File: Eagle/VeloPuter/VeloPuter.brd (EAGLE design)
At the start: 99.1 x 61 mm, 39 parts, among them IC1 LM2931T-L

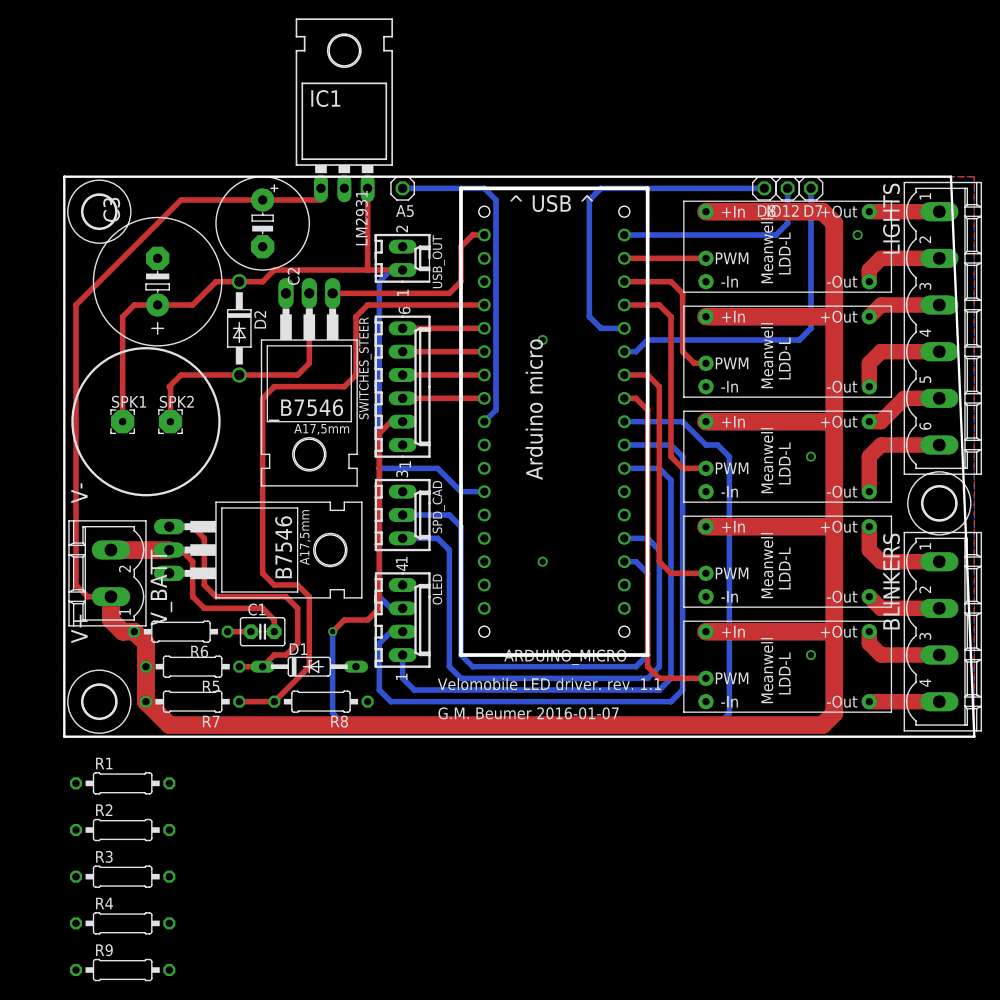
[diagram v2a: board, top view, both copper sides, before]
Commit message: new board layout
has to be checked. Pin changes NOT documented
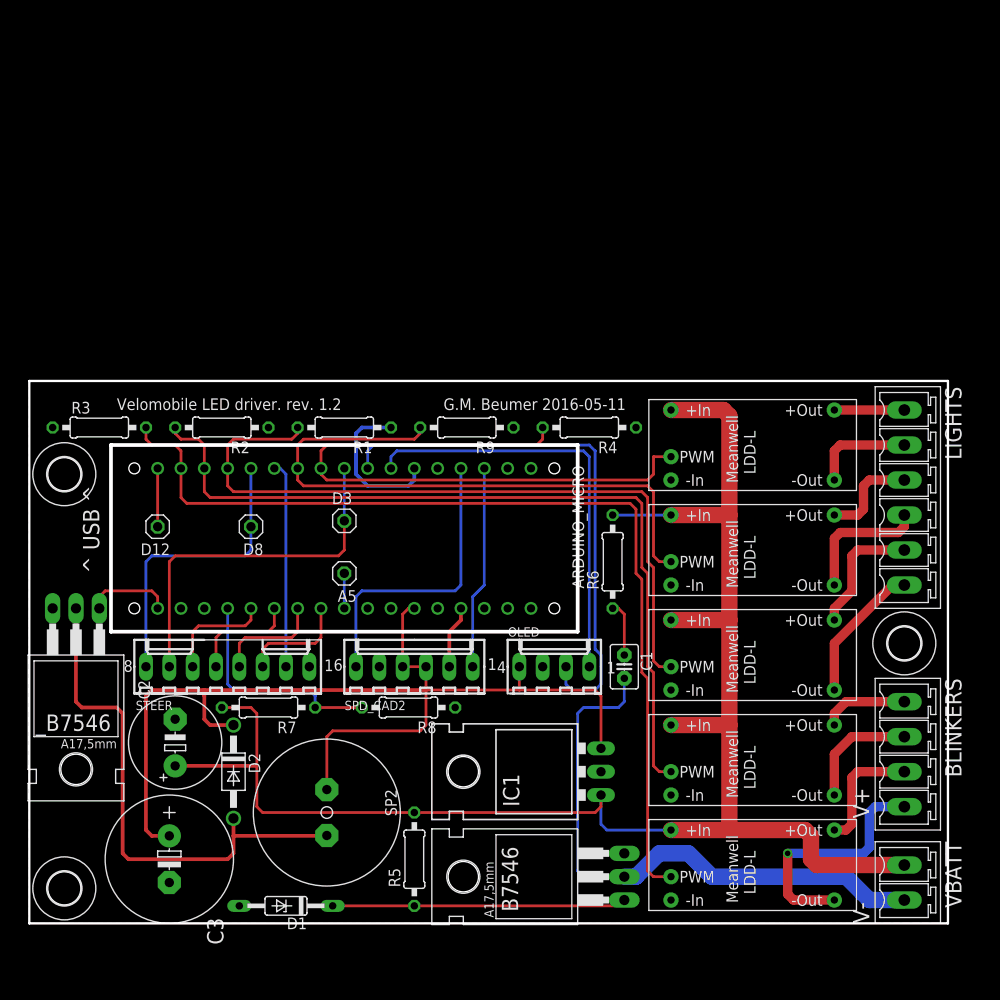
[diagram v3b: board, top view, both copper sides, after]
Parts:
- removed D7, IO12: (no value), pinhead:1X01
- removed SPD_CAD: (no value), con-molex:6410-03
- removed SPK1, SPK2: 0, wirepad:2,54/0,8
- removed SWITCHES_STEER: (no value), con-molex:6410-06
- removed USB_OUT: (no value), con-molex:6410-02
- removed V_BATT: (no value), con-phoenix-508:MSTBV2
- added D12: D12, pinhead:1X01
- added D3: D3, pinhead:1X01
- added SP2: SD1607, TDK_SD1607:AL60P
- added SPD_CAD2: 22-27-2061-06, con-molex:6410-06
- added STEER: 22-27-2081-08, con-molex:6410-08
- added VBATT: MCV2, con-phoenix_3.81_mcv:MCV2
- BLINKERS: value (none) -> 0; device con-phoenix-508:MSTBV4 -> con-phoenix_3.81_mcv:MCV4
- D8: value (none) -> D8
- LIGHTS: value (none) -> 0; device con-phoenix-508:MSTBV6 -> con-phoenix_3.81_mcv:MCV6
- moved R4 74.1 mm to (61.0, 54.0), turned to 180 degrees
- moved IC1 71.5 mm to (58.4, 16.5), turned to 90 degrees
- moved R9 69.9 mm to (47.6, 54.0), turned to 180 degrees
- moved D8 66.9 mm to (24.1, 43.2)
- moved C3 62.9 mm to (15.2, 6.99), turned to 270 degrees
- moved ARDUINO_MICRO 59.1 mm to (12.7, 50.8), turned to 270 degrees
- moved C2 57.3 mm to (15.9, 19.7), turned to 90 degrees
- moved B7546 51.2 mm to (58.4, 5.08), turned to 90 degrees
- moved R3 49.0 mm to (7.62, 54.0)
- moved D2 48.3 mm to (22.2, 16.5)
- moved R6 47.6 mm to (63.5, 39.4), turned to 90 degrees
- moved R1 45.6 mm to (34.3, 54.0), turned to 180 degrees
- moved R2 45.1 mm to (21.0, 54.0), turned to 180 degrees
- moved _B7546 42.7 mm to (5.08, 27.9)
- moved A5 42.4 mm to (34.3, 38.1)
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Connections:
- net A5 renamed FREE_A5
- removed net IO12: ARDUINO_MICRO.D12, IO12.1
- removed net N$16: ARDUINO_MICRO.D7, D7.1
- removed net N$17: ARDUINO_MICRO.D8, D8.1
- new net FREE_D12: ARDUINO_MICRO.D12, D12.1
- new net FREE_D4: ARDUINO_MICRO.D4, D3.1, STEER.7
- new net FREE_D8: ARDUINO_MICRO.D8, D8.1, STEER.8
- net 5V: now also OLED.4, SP2.1, SPD_CAD2.3, SPD_CAD2.4; no longer OLED.3, SPK1.1, USB_OUT.1
- net BRAKE_SWITCH: now also ARDUINO_MICRO.D7, STEER.2; no longer ARDUINO_MICRO.D4, SWITCHES_STEER.2
- net CAD_SWITCH: now also SPD_CAD2.6; no longer SPD_CAD.1
- net DOWN_SWITCH: now also STEER.4; no longer SWITCHES_STEER.4
- net GND: now also OLED.3, SPD_CAD2.2, SPD_CAD2.5, STEER.1; no longer OLED.4, SPD_CAD.3, SWITCHES_STEER.1, USB_OUT.2
- net LEFT_SWITCH: now also STEER.5; no longer SWITCHES_STEER.5
- net N$14: now also SP2.2; no longer SPK2.1
- net N$2: now also VBATT.2; no longer V_BATT.2
- net PWM_FRONT1: now also ARDUINO_MICRO.D5; no longer ARDUINO_MICRO.D11
- net PWM_FRONT2: now also ARDUINO_MICRO.D6; no longer ARDUINO_MICRO.D10
- net PWM_LEFT: now also ARDUINO_MICRO.D10; no longer ARDUINO_MICRO.D6
- net PWM_RIGHT: now also ARDUINO_MICRO.D11; no longer ARDUINO_MICRO.D5
- net RIGHT_SWITCH: now also STEER.6; no longer SWITCHES_STEER.6
- net UP_SWITCH: now also STEER.3; no longer SWITCHES_STEER.3
- net V+: now also VBATT.1; no longer V_BATT.1
- net WHEEL_SWITCH: now also SPD_CAD2.1; no longer SPD_CAD.2
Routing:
- net V+: track 281.5 -> 179.6 mm
- net BRAKE_SWITCH: track 122.3 -> 22.5 mm, vias 1 -> 0
- net PWM_RIGHT: track 37.9 -> 103.4 mm
- net PWM_FRONT1: track 8.89 -> 69.6 mm
- net PWM_LEFT: track 29.0 -> 88.8 mm
- net PWM_BRAKE: track 25.2 -> 79.7 mm
- net PWM_FRONT2: track 16.3 -> 66.7 mm
- net V_0: track 74.1 -> 24.7 mm
- net FREE_D4: track 0.00 -> 39.9 mm
- net N$2: track 24.4 -> 64.3 mm
- net N$16: track 36.6 -> 0.00 mm
- net N$17: track 36.6 -> 0.00 mm
- net FREE_D8: track 0.00 -> 32.3 mm
- net WHEEL_SWITCH: track 54.2 -> 22.1 mm
- net FREE_A5: track 35.3 -> 3.81 mm
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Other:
- board size 99.1 x 61 mm -> 100 x 59 mm
- board text added: "G.M. Beumer 2016-05-11"
- board text added: "Velomobile LED driver. rev. 1.2"
- board text removed: "Arduino micro"
- board text removed: "D4"
- board text removed: "D7"
- board text removed: "G.M. Beumer 2016-01-07"
- board text removed: "IO12"
- board text removed: "IO8"
- board text removed: "LM2931"
- board text removed: "NC7"
- board text removed: "NC8"
- board text removed: "Velomobile LED driver. rev. 1.1"
- board text removed: "led+"
- board text removed: "led-"

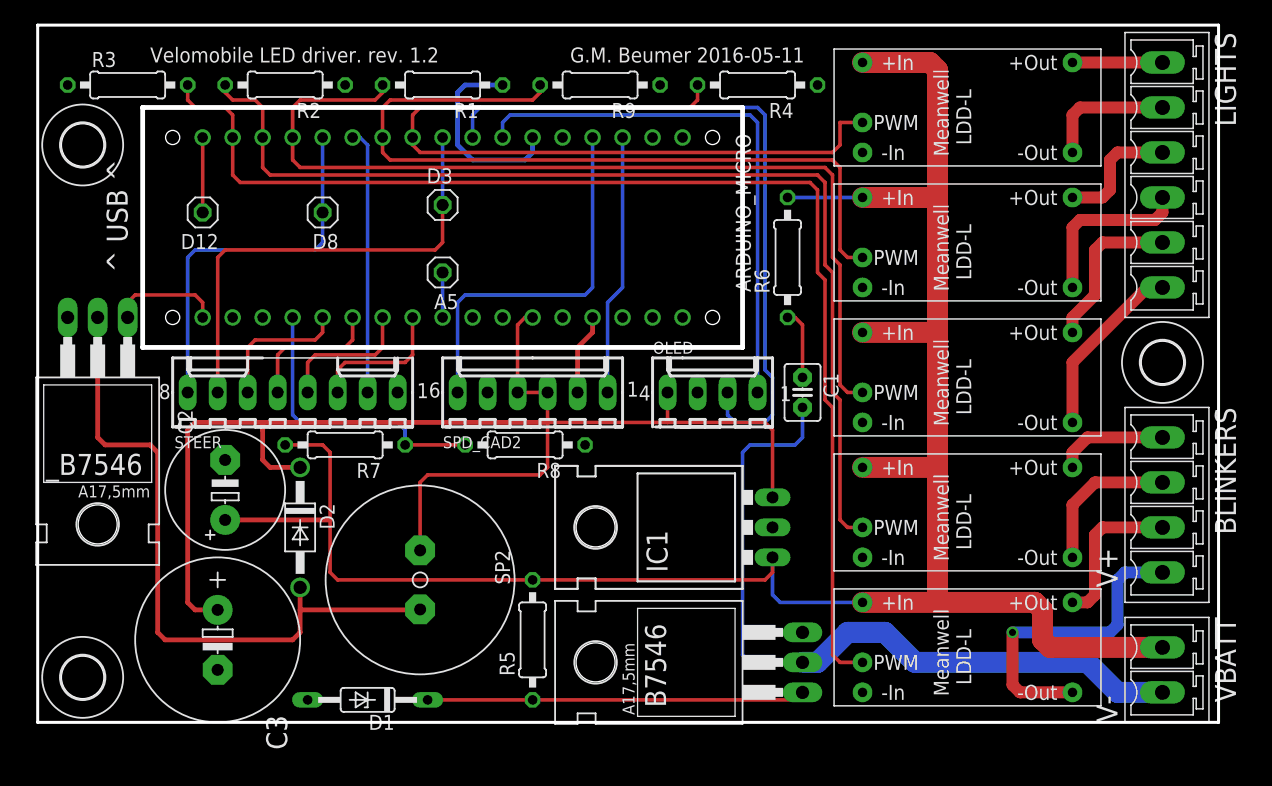
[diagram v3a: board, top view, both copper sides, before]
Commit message: Version of the Veloputer PCB as made as version 1.2 (number of the PCB).
This version is uploaded to seeedstudio.com on 2016-02-21.
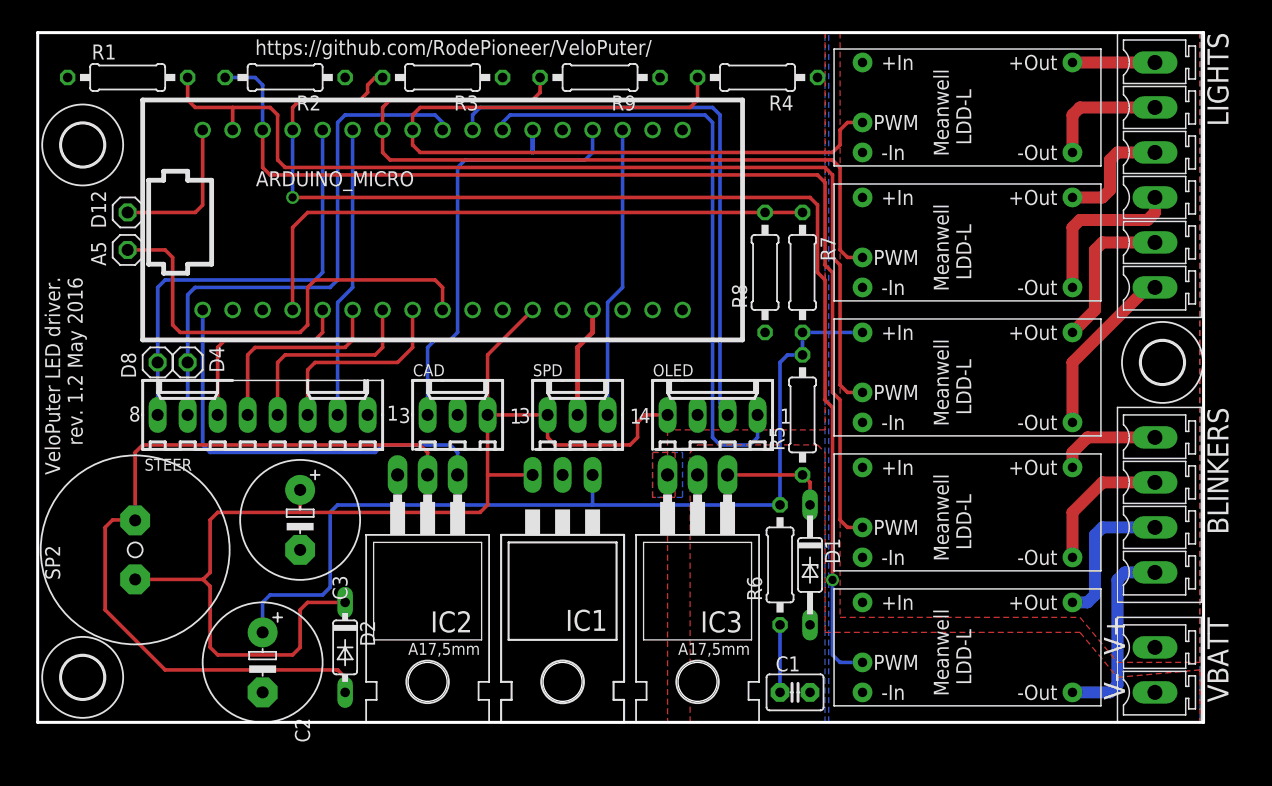
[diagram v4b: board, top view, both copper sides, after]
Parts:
- removed B7546, _B7546: (no value), transistor-power:TO220BH
- removed D3: D3, pinhead:1X01
- removed SPD_CAD2: 22-27-2061-06, con-molex:6410-06
- added CAD, SPD: 22-27-2031-03, con-molex:6410-03
- added D4: (no value), pinhead:1X01
- added IC2, IC3: B7546, transistor-power:TO220BH
- A5: value A5 -> (none)
- ARDUINO_MICRO: value (none) -> ARDUINO_MICROFOOTPRINT; device arduino-micro:ARDUINO-MICRO -> arduino-micro_gbeu:ARDUINO-MICRO
- BLINKERS, LIGHTS: value 0 -> (none)
- C3: device resistor:E5-13 -> resistor:E5-10,5
- D12: value D12 -> (none)
- D2: device diode:DO41-10 -> diode:DO35-7
- D8: value D8 -> (none)
- IC1: value LM2931T-L -> LM2931; device v-reg-3:TO220L1 -> v-reg-3-gbeu:TO220L1
- R9: value 100l -> 100k
- STEER: value 22-27-2081-08 -> (none)
- VBATT: value MCV2 -> (none)
- moved R7 41.4 mm to (64.8, 38.1), turned to 270 degrees
- moved D1 39.2 mm to (65.4, 13.3), turned to 270 degrees
- moved R5 29.8 mm to (64.8, 26.0)
- moved A5 26.7 mm to (7.62, 40.0), turned to 90 degrees
- moved R1 26.7 mm to (7.62, 54.6), turned to 0 degrees
- moved R3 26.7 mm to (34.3, 54.6), turned to 180 degrees
- moved R6 26.0 mm to (62.9, 13.3)
- moved C1 25.4 mm to (64.1, 2.54), turned to 0 degrees
- moved R8 25.0 mm to (61.6, 38.1), turned to 90 degrees
- moved SP2 24.3 mm to (8.26, 14.6), turned to 90 degrees
- moved D8 18.9 mm to (10.2, 30.5), turned to 90 degrees
- moved C2 14.9 mm to (19.1, 5.08), turned to 270 degrees
- moved IC1 14.1 mm to (44.5, 14.6), turned to 180 degrees
- moved C3 12.3 mm to (22.2, 17.1)
- moved D2 10.9 mm to (26.0, 6.35)
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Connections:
- removed net N$2: B7546.D, C1.2, VBATT.2
- new net V-: C1.2, IC3.D, VBATT.2
- net 5V: now also CAD.1, SPD.3; no longer SPD_CAD2.3, SPD_CAD2.4
- net CAD_SWITCH: now also CAD.3; no longer SPD_CAD2.6
- net FREE_D4: now also D4.1; no longer D3.1
- net GND: now also CAD.2, IC2.S, IC3.S, SPD.2; no longer B7546.S, SPD_CAD2.2, SPD_CAD2.5, _B7546.S
- net N$14: now also IC2.D; no longer _B7546.D
- net N$4: now also IC3.G; no longer B7546.G
- net PWM_BRAKE: now also ARDUINO_MICRO.D11; no longer ARDUINO_MICRO.D9
- net PWM_BUZZER: now also IC2.G; no longer _B7546.G
- net PWM_RIGHT: now also ARDUINO_MICRO.D9; no longer ARDUINO_MICRO.D11
- net WHEEL_SWITCH: now also SPD.1; no longer SPD_CAD2.1
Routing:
- net V+: track 179.6 -> 77.3 mm
- net N$2: track 64.3 -> 0.00 mm
- net FREE_A5: track 3.81 -> 38.8 mm
- net PWM_BUZZER: track 9.42 -> 35.7 mm
- net V_0: track 24.7 -> 50.7 mm
- net N$4: track 32.0 -> 9.15 mm
- net 5V: track 115.5 -> 99.5 mm
- net GND: track 23.8 -> 11.3 mm
- net SCL_OLED: track 59.1 -> 48.4 mm
- net N$9: track 26.8 -> 16.4 mm, vias 1 -> 0
- net N$14: track 57.6 -> 66.7 mm
- net FREE_D4: track 39.9 -> 46.8 mm
- net FREE_D12: track 6.35 -> 13.0 mm
- net SDA_OLED: track 46.2 -> 51.9 mm
- net FREE_D8: track 32.3 -> 37.4 mm
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- added copper zone on layer 1, net V+
- added copper zone on layer 1, net V-
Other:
- board size 100 x 59 mm -> 98.7 x 58.4 mm
- board text added: "VeloPuter LED driver. rev. 1.2 May 2016"
- board text added: "https://github.com/RodePioneer/VeloPuter/"
- board text removed: "G.M. Beumer 2016-05-11"
- board text removed: "Velomobile LED driver. rev. 1.2"
- board text removed: "^ USB ^"

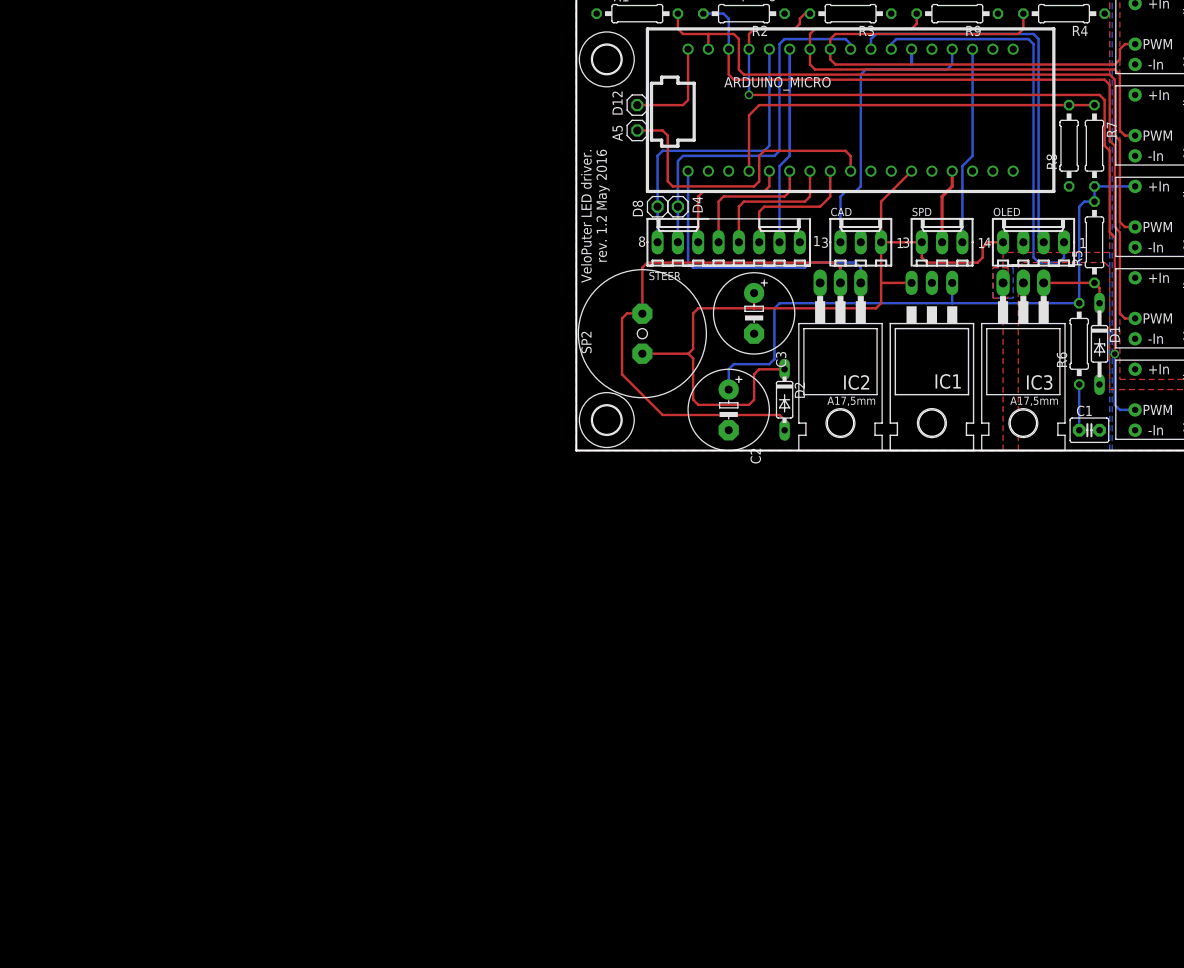
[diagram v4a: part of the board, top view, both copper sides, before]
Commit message: Started working on the PCB again. Adding swtichoff of the ALL Ldd's. Also: adding a 6th LDDd.
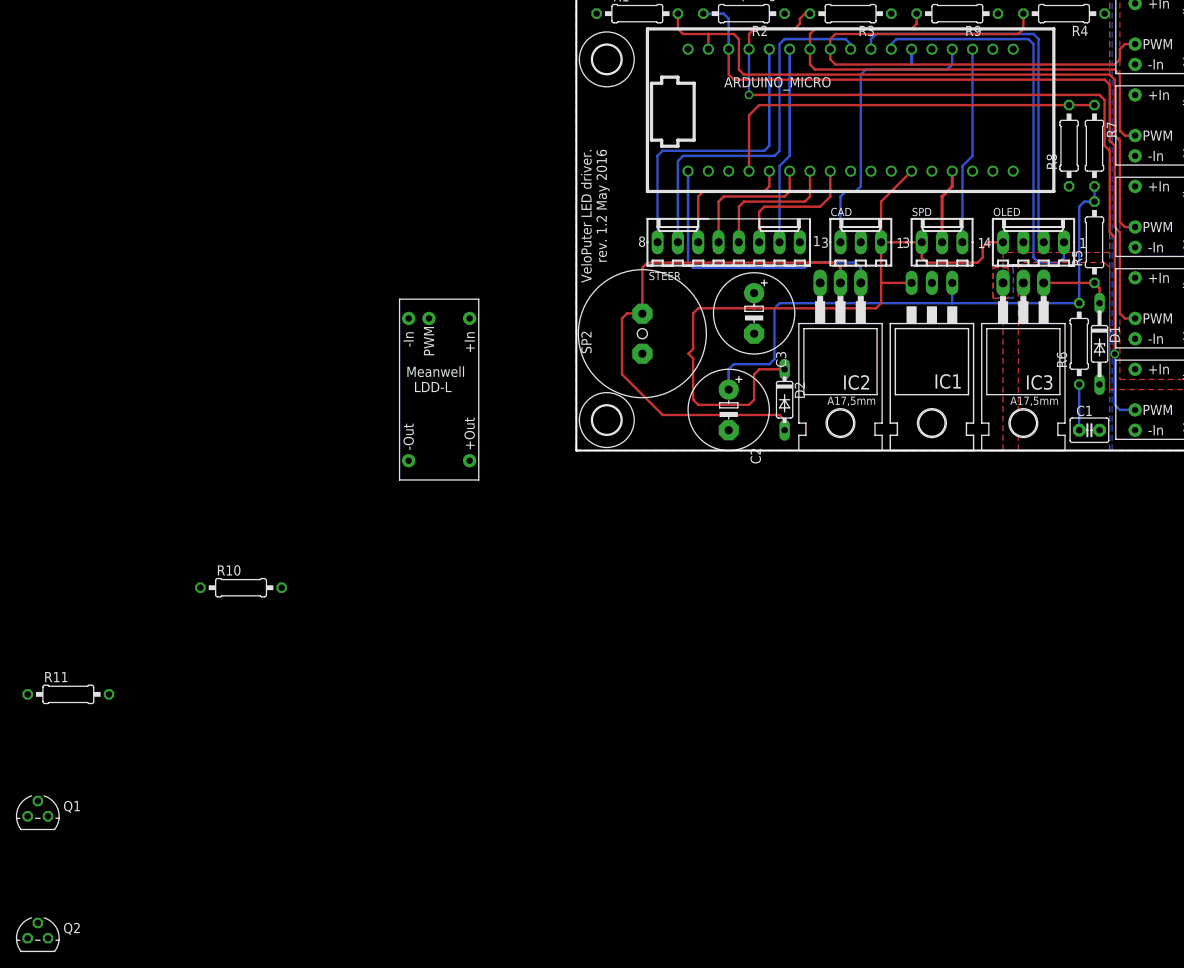
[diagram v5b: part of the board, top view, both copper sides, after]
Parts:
- removed A5, D12, D4, D8: (no value), pinhead:1X01
- added Q1: BSS92, transistor-fet:TO92
- added Q2: BSS101, transistor-fet:TO92
- added R10, R11: 100k, resistor:0207/10
- added U$1: (no value), meanwell_dcdc:LDD-L
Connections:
- net PWM_BRAKE renamed PWM_REAR
- net PWM_FRONT1 renamed PWM_FRONT
- net PWM_FRONT2 renamed PWM_AUX1
- removed net FREE_A5: A5.1, ARDUINO_MICRO.A5
- removed net FREE_D12: ARDUINO_MICRO.D12, D12.1
- removed net FREE_D4: ARDUINO_MICRO.D4, D4.1, STEER.7
- removed net FREE_D8: ARDUINO_MICRO.D8, D8.1, STEER.8
- new net ALARM_SWITCH: ARDUINO_MICRO.D8, STEER.8
- new net CONFIG_SWITCH: ARDUINO_MICRO.D4, STEER.7
- new net N$15: Q1.1, Q2.3, R11.1
- new net N$20: BRAKE.+VIN
- new net ONOFF: ARDUINO_MICRO.A5, Q2.2
- new net ONOFF_AUX2: ARDUINO_MICRO.D12, R10.2, U$1.PWM
- new net VDD: Q1.3, U$1.+VIN, U$2.+VIN, U$3.+VIN, U$4.+VIN, U$5.+VIN
- net GND: now also Q2.1, R10.1, U$1.-VIN
- net V+: now also Q1.2, R11.2; no longer BRAKE.+VIN, U$2.+VIN, U$3.+VIN, U$4.+VIN, U$5.+VIN
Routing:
- net FREE_D4: track 46.8 -> 0.00 mm
- net CONFIG_SWITCH: track 0.00 -> 46.8 mm
- net FREE_A5: track 38.8 -> 0.00 mm
- net FREE_D8: track 37.4 -> 0.00 mm
- net ALARM_SWITCH: track 0.00 -> 37.4 mm
- net FREE_D12: track 13.0 -> 0.00 mm
- net 5V: track 99.5 -> 93.7 mm
- net V+: track 77.3 -> 72.2 mm
